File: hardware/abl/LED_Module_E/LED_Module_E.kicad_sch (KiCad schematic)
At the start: 90 parts, among them J1 SFW20S-2STE1LF, J3 009159008603906, Q1 Si3456DDV, Q11 Si3456DDV, Q12 Si3456DDV, Q2 Si3456DDV, Q3 Si3456DDV, Q4 Si3456DDV, Q5 Si3456DDV, Q6 Si3456DDV, Q7 Si3456DDV, Q8 Si3456DDV, U1 TMP1075DGK, U2 74HC245, U3 24AA02UIDT-I/OT

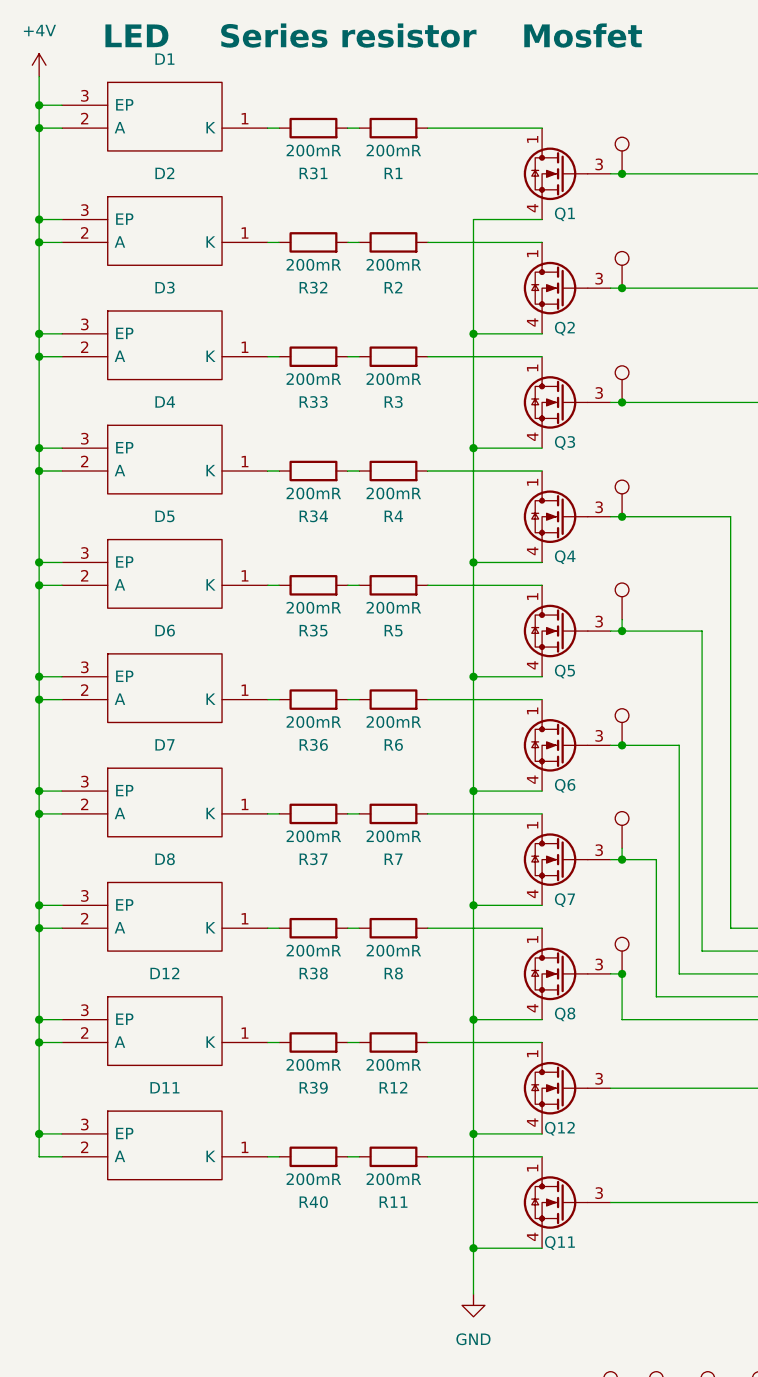
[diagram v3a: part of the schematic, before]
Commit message: Re-numbered resistors.
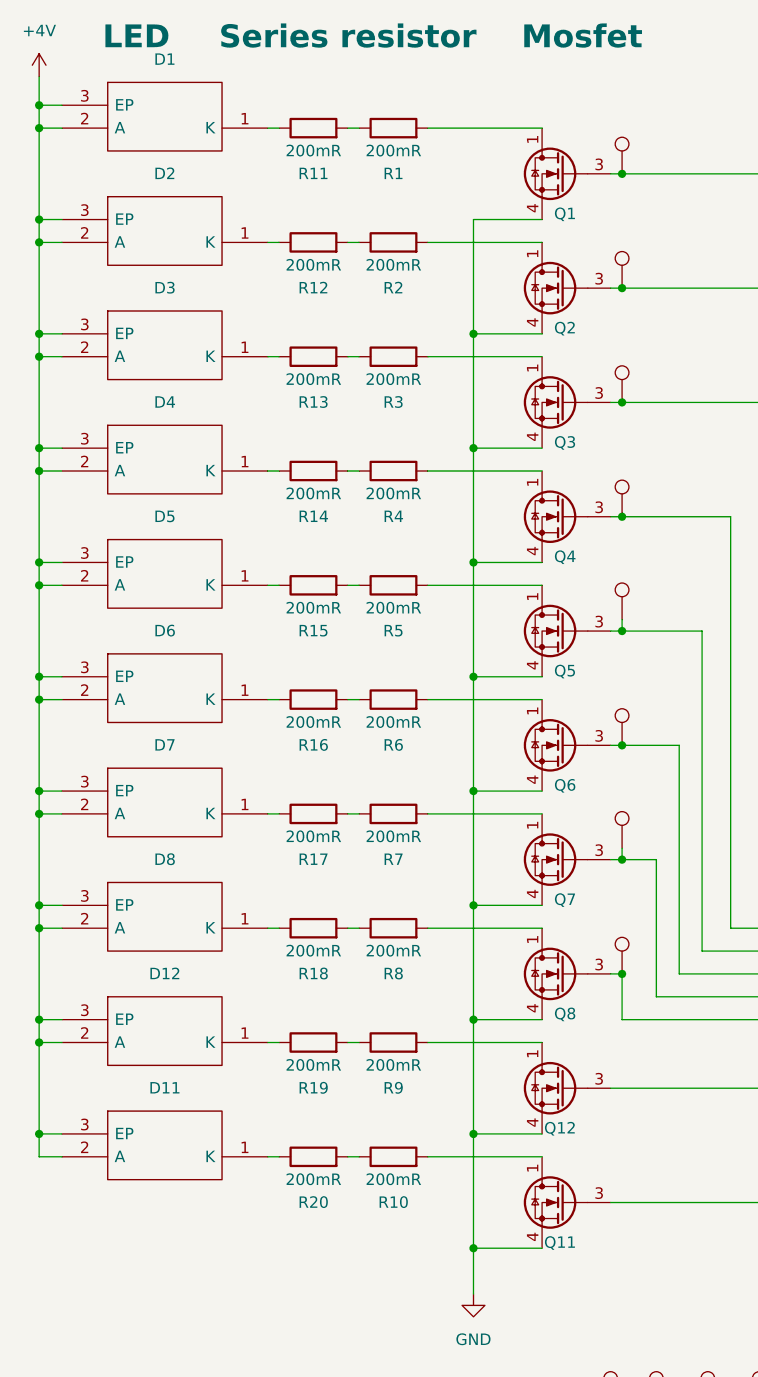
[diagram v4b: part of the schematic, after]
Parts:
- renumbered R11 to R10, R31 to R11, R32 to R12, R33 to R13, R34 to R14, R35 to R15, R36 to R16, R37 to R17, R38 to R18, R39 to R19, R40 to R20, R9 to R21, R10 to R22, R13 to R23, R14 to R24, R15 to R25, R16 to R26, R17 to R27, R18 to R28, R20 to R31, R21 to R32, R22 to R33, R23 to R34, R24 to R35, R25 to R36, R26 to R37, R27 to R38, R28 to R40, R19 to R41, R12 to R9
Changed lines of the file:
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@@
 		(on_board yes)
 		(dnp no)
-		(property "Reference" "R38"
+		(property "Reference" "R18"
 			(at 67.31 121.92 90)
 			(effects
@@
 			(project "LED_Module_E"
 				(path "/271a71a9-d0cc-4466-ad75-113fb931f3c8"
-					(reference "R38")
+					(reference "R18")
 					(unit 1)
 				)
@@
 		(on_board yes)
 		(dnp no)
-		(property "Reference" "R11"
+		(property "Reference" "R10"
 			(at 76.2 147.32 90)
 			(effects
@@
 			(project "LED_Module_E"
 				(path "/271a71a9-d0cc-4466-ad75-113fb931f3c8"
-					(reference "R11")
+					(reference "R10")
 					(unit 1)
 				)
@@
 		(dnp no)
 		(fields_autoplaced yes)
-		(property "Reference" "R19"
+		(property "Reference" "R41"
 			(at 180.3399 136.525 0)
 			(effects
@@
 			(project "LED_Module_E"
 				(path "/271a71a9-d0cc-4466-ad75-113fb931f3c8"
-					(reference "R19")
+					(reference "R41")
 					(unit 1)
 				)
@@
 		(dnp no)
 		(fields_autoplaced yes)
-		(property "Reference" "R22"
+		(property "Reference" "R33"
 			(at 135.89 132.0799 0)
 			(effects
@@
 			(project "LED_Module_E"
 				(path "/271a71a9-d0cc-4466-ad75-113fb931f3c8"
-					(reference "R22")
+					(reference "R33")
 					(unit 1)
 				)
@@
 		(dnp no)
 		(fields_autoplaced yes)
-		(property "Reference" "R23"
+		(property "Reference" "R34"
 			(at 138.43 132.0799 0)
 			(effects
@@
 			(project "LED_Module_E"
 				(path "/271a71a9-d0cc-4466-ad75-113fb931f3c8"
-					(reference "R23")
+					(reference "R34")
 					(unit 1)
 				)
@@
 		(on_board yes)
 		(dnp no)
-		(property "Reference" "R34"
+		(property "Reference" "R14"
 			(at 67.31 71.12 90)
 			(effects
@@
 			(project "LED_Module_E"
 				(path "/271a71a9-d0cc-4466-ad75-113fb931f3c8"
-					(reference "R34")
+					(reference "R14")
 					(unit 1)
 				)
@@
 		(dnp no)
 		(fields_autoplaced yes)
-		(property "Reference" "R16"
+		(property "Reference" "R26"
 			(at 183.5149 124.46 0)
 			(effects
@@
 			(project "LED_Module_E"
 				(path "/271a71a9-d0cc-4466-ad75-113fb931f3c8"
-					(reference "R16")
+					(reference "R26")
 					(unit 1)
 				)
@@
 		(on_board yes)
 		(dnp no)
-		(property "Reference" "R12"
+		(property "Reference" "R9"
 			(at 76.2 134.62 90)
 			(effects
@@
 			(project "LED_Module_E"
 				(path "/271a71a9-d0cc-4466-ad75-113fb931f3c8"
-					(reference "R12")
+					(reference "R9")
 					(unit 1)
 				)
@@
 		(dnp no)
 		(fields_autoplaced yes)
-		(property "Reference" "R27"
+		(property "Reference" "R38"
 			(at 148.59 132.0799 0)
 			(effects
@@
 			(project "LED_Module_E"
 				(path "/271a71a9-d0cc-4466-ad75-113fb931f3c8"
-					(reference "R27")
+					(reference "R38")
 					(unit 1)
 				)
@@
 		(dnp no)
 		(fields_autoplaced yes)
-		(property "Reference" "R14"
+		(property "Reference" "R24"
 			(at 183.5149 119.38 0)
 			(effects
@@
 			(project "LED_Module_E"
 				(path "/271a71a9-d0cc-4466-ad75-113fb931f3c8"
-					(reference "R14")
+					(reference "R24")
 					(unit 1)
 				)
@@
 		(on_board yes)
 		(dnp no)
-		(property "Reference" "R37"
+		(property "Reference" "R17"
 			(at 67.31 109.22 90)
 			(effects
@@
 			(project "LED_Module_E"
 				(path "/271a71a9-d0cc-4466-ad75-113fb931f3c8"
-					(reference "R37")
+					(reference "R17")
 					(unit 1)
 				)
@@
 		(dnp no)
 		(fields_autoplaced yes)
-		(property "Reference" "R28"
+		(property "Reference" "R40"
 			(at 220.98 28.5749 0)
 			(effects
@@
 			(project "LED_Module_E"
 				(path "/271a71a9-d0cc-4466-ad75-113fb931f3c8"
-					(reference "R28")
+					(reference "R40")
 					(unit 1)
 				)
@@
 		(dnp no)
 		(fields_autoplaced yes)
-		(property "Reference" "R17"
+		(property "Reference" "R27"
 			(at 183.5149 127 0)
 			(effects
@@
 			(project "LED_Module_E"
 				(path "/271a71a9-d0cc-4466-ad75-113fb931f3c8"
-					(reference "R17")
+					(reference "R27")
 					(unit 1)
 				)
@@
 		(on_board yes)
 		(dnp no)
-		(property "Reference" "R36"
+		(property "Reference" "R16"
 			(at 67.31 96.52 90)
 			(effects
@@
 			(project "LED_Module_E"
 				(path "/271a71a9-d0cc-4466-ad75-113fb931f3c8"
-					(reference "R36")
+					(reference "R16")
 					(unit 1)
 				)
@@
 		(dnp no)
 		(fields_autoplaced yes)
-		(property "Reference" "R13"
+		(property "Reference" "R23"
 			(at 183.5149 116.84 0)
 			(effects
@@
 			(project "LED_Module_E"
 				(path "/271a71a9-d0cc-4466-ad75-113fb931f3c8"
-					(reference "R13")
+					(reference "R23")
 					(unit 1)
 				)
@@
 		(dnp no)
 		(fields_autoplaced yes)
-		(property "Reference" "R20"
+		(property "Reference" "R31"
 			(at 130.81 132.0799 0)
 			(effects
@@
 			(project "LED_Module_E"
 				(path "/271a71a9-d0cc-4466-ad75-113fb931f3c8"
-					(reference "R20")
+					(reference "R31")
 					(unit 1)
 				)
@@
 		(on_board yes)
 		(dnp no)
-		(property "Reference" "R35"
+		(property "Reference" "R15"
 			(at 67.31 83.82 90)
 			(effects
@@
 			(project "LED_Module_E"
 				(path "/271a71a9-d0cc-4466-ad75-113fb931f3c8"
-					(reference "R35")
+					(reference "R15")
 					(unit 1)
 				)
@@
 		(on_board yes)
 		(dnp no)
-		(property "Reference" "R40"
+		(property "Reference" "R20"
 			(at 67.31 147.32 90)
 			(effects
@@
 			(project "LED_Module_E"
 				(path "/271a71a9-d0cc-4466-ad75-113fb931f3c8"
-					(reference "R40")
+					(reference "R20")
 					(unit 1)
 				)
@@
 		(dnp no)
 		(fields_autoplaced yes)
-		(property "Reference" "R25"
+		(property "Reference" "R36"
 			(at 143.51 132.0799 0)
 			(effects
@@
 			(project "LED_Module_E"
 				(path "/271a71a9-d0cc-4466-ad75-113fb931f3c8"
-					(reference "R25")
+					(reference "R36")
 					(unit 1)
 				)
@@
 		(dnp no)
 		(fields_autoplaced yes)
-		(property "Reference" "R10"
+		(property "Reference" "R22"
 			(at 183.5149 114.3 0)
 			(effects
@@
 			(project "LED_Module_E"
 				(path "/271a71a9-d0cc-4466-ad75-113fb931f3c8"
-					(reference "R10")
+					(reference "R22")
 					(unit 1)
 				)
@@
 		(on_board yes)
 		(dnp no)
-		(property "Reference" "R31"
+		(property "Reference" "R11"
 			(at 67.31 33.02 90)
 			(effects
@@
 			(project "LED_Module_E"
 				(path "/271a71a9-d0cc-4466-ad75-113fb931f3c8"
-					(reference "R31")
+					(reference "R11")
 					(unit 1)
 				)
@@
 		(dnp no)
 		(fields_autoplaced yes)
-		(property "Reference" "R21"
+		(property "Reference" "R32"
 			(at 133.35 132.0799 0)
 			(effects
@@
 			(project "LED_Module_E"
 				(path "/271a71a9-d0cc-4466-ad75-113fb931f3c8"
-					(reference "R21")
+					(reference "R32")
 					(unit 1)
 				)
@@
 		(dnp no)
 		(fields_autoplaced yes)
-		(property "Reference" "R24"
+		(property "Reference" "R35"
 			(at 140.97 132.0799 0)
 			(effects
@@
 			(project "LED_Module_E"
 				(path "/271a71a9-d0cc-4466-ad75-113fb931f3c8"
-					(reference "R24")
+					(reference "R35")
 					(unit 1)
 				)
@@
 		(on_board yes)
 		(dnp no)
-		(property "Reference" "R32"
+		(property "Reference" "R12"
 			(at 67.31 45.72 90)
 			(effects
@@
 			(project "LED_Module_E"
 				(path "/271a71a9-d0cc-4466-ad75-113fb931f3c8"
-					(reference "R32")
+					(reference "R12")
 					(unit 1)
 				)
@@
 		(dnp no)
 		(fields_autoplaced yes)
-		(property "Reference" "R9"
+		(property "Reference" "R21"
 			(at 183.5149 111.76 0)
 			(effects
@@
 			(project "LED_Module_E"
 				(path "/271a71a9-d0cc-4466-ad75-113fb931f3c8"
-					(reference "R9")
+					(reference "R21")
 					(unit 1)
 				)
@@
 		(dnp no)
 		(fields_autoplaced yes)
-		(property "Reference" "R26"
+		(property "Reference" "R37"
 			(at 146.05 132.0799 0)
 			(effects
@@
 			(project "LED_Module_E"
 				(path "/271a71a9-d0cc-4466-ad75-113fb931f3c8"
-					(reference "R26")
+					(reference "R37")
 					(unit 1)
 				)
@@
 		(dnp no)
 		(fields_autoplaced yes)
-		(property "Reference" "R15"
+		(property "Reference" "R25"
 			(at 183.5149 121.92 0)
 			(effects
@@
 			(project "LED_Module_E"
 				(path "/271a71a9-d0cc-4466-ad75-113fb931f3c8"
-					(reference "R15")
+					(reference "R25")
 					(unit 1)
 				)
@@
 		(on_board yes)
 		(dnp no)
-		(property "Reference" "R33"
+		(property "Reference" "R13"
 			(at 67.31 58.42 90)
 			(effects
@@
 			(project "LED_Module_E"
 				(path "/271a71a9-d0cc-4466-ad75-113fb931f3c8"
-					(reference "R33")
+					(reference "R13")
 					(unit 1)
 				)
@@
 		(on_board yes)
 		(dnp no)
-		(property "Reference" "R39"
+		(property "Reference" "R19"
 			(at 67.31 134.62 90)
 			(effects
@@
 			(project "LED_Module_E"
 				(path "/271a71a9-d0cc-4466-ad75-113fb931f3c8"
-					(reference "R39")
+					(reference "R19")
 					(unit 1)
 				)
@@
 		(dnp no)
 		(fields_autoplaced yes)
-		(property "Reference" "R18"
+		(property "Reference" "R28"
 			(at 183.5149 129.54 0)
 			(effects
@@
 			(project "LED_Module_E"
 				(path "/271a71a9-d0cc-4466-ad75-113fb931f3c8"
-					(reference "R18")
+					(reference "R28")
 					(unit 1)
 				)

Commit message: Fixed a few footprints and part numbers.
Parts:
- C1: LCSC Part # (none) -> C1525
- C2, C3: footprint Capacitor_SMD:C_0603_1608Metric_Pad1.08x0.95mm_HandSolder -> Capacitor_SMD:C_0402_1005Metric; LCSC Part # (none) -> C1525
- U2: LCSC Part # (none) -> C10910; Manufacturer_Part_Number (none) -> SN74AHCT245PWR
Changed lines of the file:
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@@
 			)
 		)
+		(property "LCSC Part #" "C10910"
+			(at 163.83 121.92 0)
+			(effects
+				(font
+					(size 1.27 1.27)
+				)
+				(hide yes)
+			)
+		)
+		(property "Manufacturer_Part_Number" "SN74AHCT245PWR"
+			(at 163.83 121.92 0)
+			(effects
+				(font
+					(size 1.27 1.27)
+				)
+				(hide yes)
+			)
+		)
 		(pin "7"
 		)
@@
 			)
 		)
-		(property "LCSC Part #" ""
+		(property "LCSC Part #" "C1525"
 			(at 193.675 48.895 0)
 			(effects
@@
 			)
 		)
-		(property "Footprint" "Capacitor_SMD:C_0603_1608Metric_Pad1.08x0.95mm_HandSolder"
+		(property "Footprint" "Capacitor_SMD:C_0402_1005Metric"
 			(at 240.03 46.99 0)
 			(effects
@@
 			)
 		)
-		(property "LCSC Part #" ""
+		(property "LCSC Part #" "C1525"
 			(at 240.03 46.99 0)
 			(effects
@@
 			)
 		)
-		(property "Footprint" "Capacitor_SMD:C_0603_1608Metric_Pad1.08x0.95mm_HandSolder"
+		(property "Footprint" "Capacitor_SMD:C_0402_1005Metric"
 			(at 168.275 99.06 0)
 			(effects
@@
 			)
 		)
-		(property "LCSC Part #" ""
+		(property "LCSC Part #" "C1525"
 			(at 168.275 99.06 0)
 			(effects

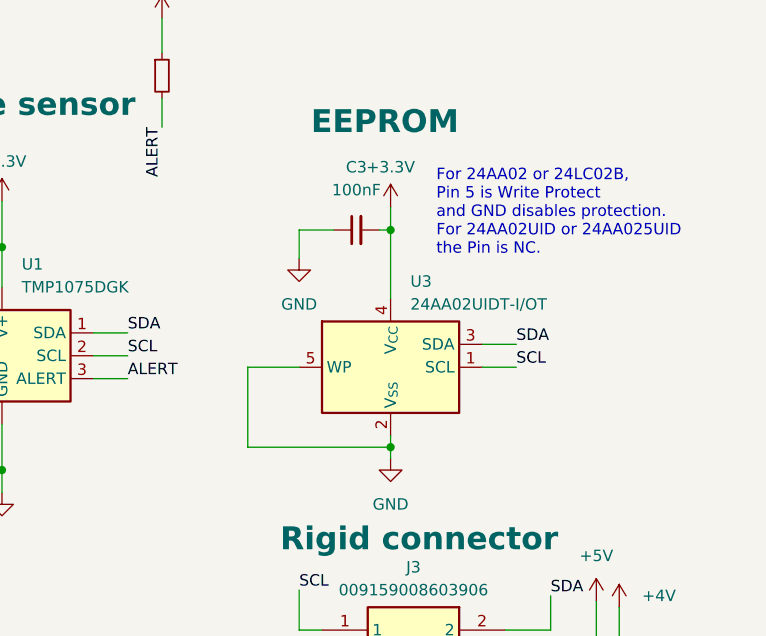
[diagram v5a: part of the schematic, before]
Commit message: Added an EEPROM to the power module and changed the EEPROM on the LED module to be individually addressable.
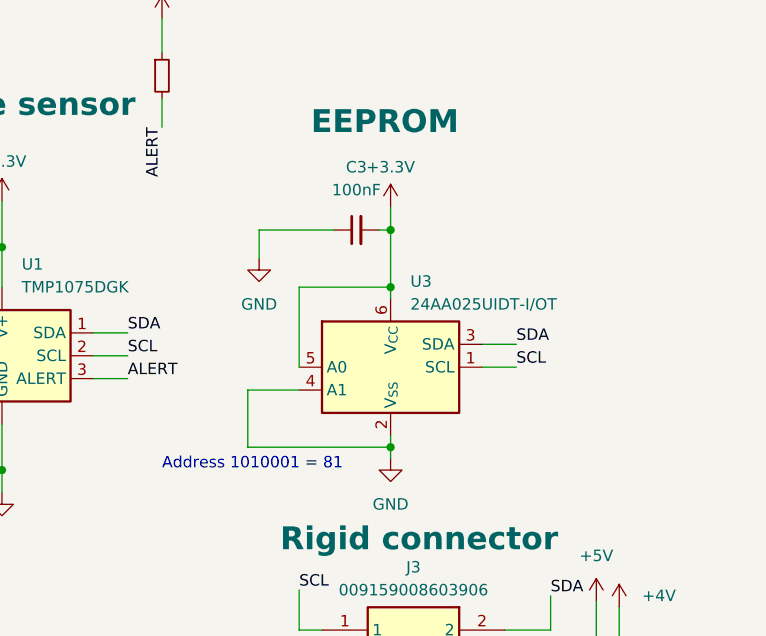
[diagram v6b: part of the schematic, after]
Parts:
- U3: value 24AA02UIDT-I/OT -> 24AA025UIDT-I/OT; footprint Package_TO_SOT_SMD:SOT-23-5 -> Package_TO_SOT_SMD:SOT-23-6; symbol Memory_EEPROM:24AA02-OT -> Memory_EEPROM:24AA02XEXX; LCSC Part # C511274 -> C2061498; Manufacturer_Part_Number 24AA02UIDT-I/OT -> 24AA025UIDT-I/OT
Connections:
- net +3.3V: now also U3.5 (A0), U3.6 (V_{CC}); no longer U3.4 (V_{CC})
- net GND: now also U3.4 (A1); no longer U3.5 (WP)
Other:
- note added: "Address 1010001 = 81"
- note removed: "For 24AA02 or 24LC02B, Pin 5 is Write Protect and GND disables protection. For 24AA02UID or 24AA025UID the Pin is NC."
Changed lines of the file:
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@@
 	(title_block
 		(title "besteLampe! LED Module E")
-		(date "2024-09-15")
-		(rev "2.0")
+		(date "2024-11-01")
+		(rev "2.1")
 		(comment 1 "See  https://lenaschimmel.de/besteLampe! for the source and more information")
 		(comment 2 "This source describes Open Hardware and is licensed under the CERN-OHL-S v2.")
@@
 	)
 	(junction
+		(at 243.84 53.34)
+		(diameter 0)
+		(color 0 0 0 0)
+	)
+	(junction
 		(at 36.83 40.64)
 		(diameter 0)
@@
 	(wire
 		(pts
+			(xy 233.68 53.34) (xy 243.84 53.34)
+		)
+		(stroke
+			(width 0)
+			(type default)
+		)
+	)
+	(wire
+		(pts
 			(xy 151.13 116.84) (xy 135.89 116.84)
 		)
@@
 	(wire
 		(pts
-			(xy 233.68 50.165) (xy 233.68 46.99)
+			(xy 229.235 50.165) (xy 229.235 46.99)
 		)
 		(stroke
@@
 	(wire
 		(pts
+			(xy 233.68 62.23) (xy 233.68 53.34)
+		)
+		(stroke
+			(width 0)
+			(type default)
+		)
+	)
+	(wire
+		(pts
 			(xy 219.71 135.89) (xy 219.71 139.7)
 		)
@@
 	(wire
 		(pts
-			(xy 227.965 62.23) (xy 227.965 71.12)
+			(xy 227.965 64.77) (xy 227.965 71.12)
 		)
 		(stroke
@@
 	(wire
 		(pts
-			(xy 233.68 46.99) (xy 237.49 46.99)
+			(xy 229.235 46.99) (xy 237.49 46.99)
 		)
 		(stroke
@@
 	(wire
 		(pts
-			(xy 243.84 46.99) (xy 243.84 54.61)
+			(xy 243.84 46.99) (xy 243.84 53.34)
 		)
 		(stroke
@@
 	(wire
 		(pts
+			(xy 243.84 53.34) (xy 243.84 54.61)
+		)
+		(stroke
+			(width 0)
+			(type default)
+		)
+	)
+	(wire
+		(pts
 			(xy 36.83 78.74) (xy 36.83 88.9)
 		)
@@
 	(wire
 		(pts
-			(xy 227.965 62.23) (xy 233.68 62.23)
+			(xy 227.965 64.77) (xy 233.68 64.77)
 		)
 		(stroke
@@
 		)
 	)
-	(text "For 24AA02 or 24LC02B, \nPin 5 is Write Protect \nand GND disables protection.\nFor 24AA02UID or 24AA025UID \nthe Pin is NC."
+	(text "Address 1010001 = 81"
 		(exclude_from_sim no)
-		(at 248.92 45.085 0)
+		(at 218.44 73.025 0)
 		(effects
 			(font
@@
 	)
 	(symbol
-		(lib_id "Memory_EEPROM:24AA02-OT")
+		(lib_id "Memory_EEPROM:24AA02XEXX")
 		(at 243.84 62.23 0)
 		(unit 1)
@@
 			)
 		)
-		(property "Value" "24AA02UIDT-I/OT"
+		(property "Value" "24AA025UIDT-I/OT"
 			(at 246.0341 55.245 0)
 			(effects
@@
 			)
 		)
-		(property "Footprint" "Package_TO_SOT_SMD:SOT-23-5"
-			(at 243.84 62.23 0)
+		(property "Footprint" "Package_TO_SOT_SMD:SOT-23-6"
+			(at 243.84 52.07 0)
 			(effects
 				(font
@@
 			)
 		)
-		(property "Datasheet" ""
-			(at 243.84 62.23 0)
+		(property "Datasheet" "http://ww1.microchip.com/downloads/en/DeviceDoc/21709J.pdf"
+			(at 243.84 49.53 0)
 			(effects
 				(font
@@
 		)
 		(property "Description" "I2C Serial EEPROM, 2Kb, SOT-23"
-			(at 243.84 62.23 0)
+			(at 243.84 46.99 0)
 			(effects
 				(font
@@
 			)
 		)
-		(property "Manufacturer_Part_Number" "24AA02UIDT-I/OT"
+		(property "Manufacturer_Part_Number" "24AA025UIDT-I/OT"
 			(at 243.84 62.23 0)
 			(effects
@@
 			)
 		)
-		(property "LCSC Part #" "C511274"
+		(property "LCSC Part #" "C2061498"
 			(at 243.84 62.23 0)
 			(effects
@@
 		(pin "2"
 		)
+		(pin "6"
+		)
 		(instances
 			(project "LED_Module_E"
@@
 	(symbol
 		(lib_id "power:GND")
-		(at 233.68 50.165 0)
+		(at 229.235 50.165 0)
 		(unit 1)
 		(exclude_from_sim no)
@@
 		(fields_autoplaced yes)
 		(property "Reference" "#PWR011"
-			(at 233.68 56.515 0)
+			(at 229.235 56.515 0)
 			(effects
 				(font
@@
 		)
 		(property "Value" "GND"
-			(at 233.68 55.245 0)
+			(at 229.235 55.245 0)
 			(effects
 				(font
@@
 		)
 		(property "Footprint" ""
-			(at 233.68 50.165 0)
+			(at 229.235 50.165 0)
 			(effects
 				(font
@@
 		)
 		(property "Datasheet" ""
-			(at 233.68 50.165 0)
+			(at 229.235 50.165 0)
 			(effects
 				(font
@@
 		)
 		(property "Description" "Power symbol creates a global label with name \"GND\" , ground"
-			(at 233.68 50.165 0)
+			(at 229.235 50.165 0)
 			(effects
 				(font
